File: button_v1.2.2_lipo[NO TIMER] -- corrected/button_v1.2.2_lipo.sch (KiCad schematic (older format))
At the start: 19 parts, among them J1 Conn_01x05_Female, SW1 SW_Push, SW2 SW_Push, U2 AP2112K-3.3, X1 ESP-12E

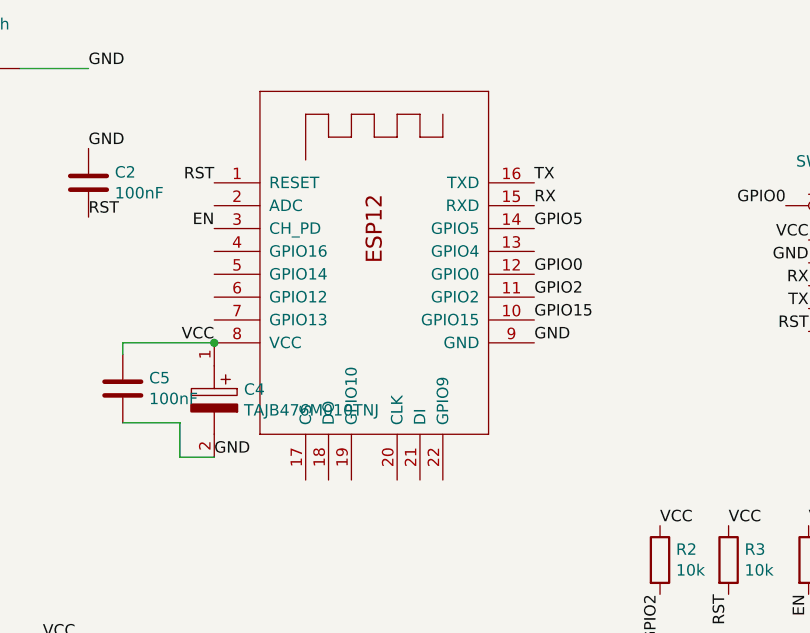
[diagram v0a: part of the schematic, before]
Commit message: All Footprints corrected
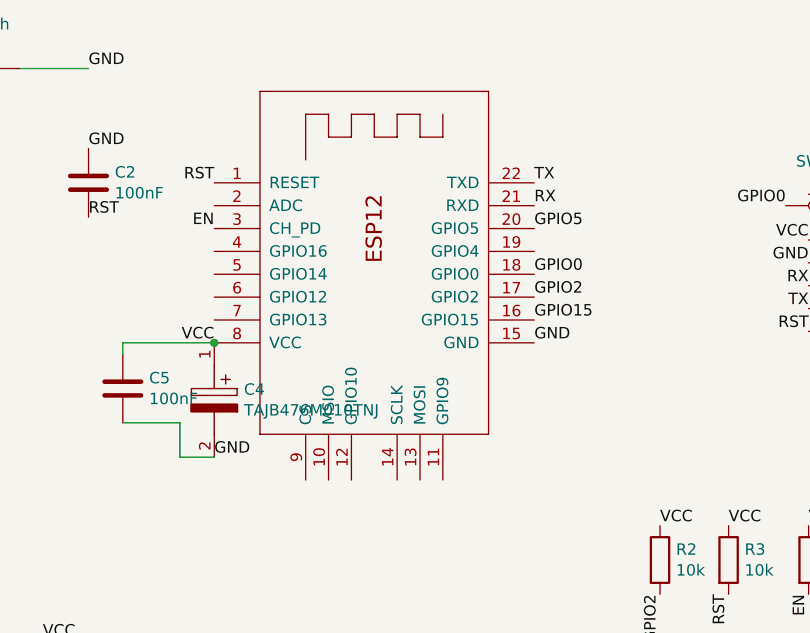
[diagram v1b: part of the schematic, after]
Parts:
- removed X1: ESP-12E, RF_Module:ESP-12E, symbol button_v1.2.2_lipo-rescue:ESP-12E-ardafruit-button-timer-rescue-button-timer-v1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
- added X1: ESP-12E, handsolder:ESP-12Elesssilk, symbol ardafruit:ESP-12E
- D1: footprint LED_SMD:LED_1206_3216Metric_Castellated -> handsolder:LED_1206_3216Metric_Castellated
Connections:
- net EN: now also X1.3 (CH_PD)
- net GND: now also X1.15 (GND)
- net GPIO0: now also X1.18 (GPIO0)
- net GPIO15: now also X1.16 (GPIO15)
- net GPIO2: now also X1.17 (GPIO2)
- net GPIO5: now also X1.20 (GPIO5)
- net RST: now also X1.1 (RESET)
- net RX: now also X1.21 (RXD)
- net TX: now also X1.22 (TXD)
- net VCC: now also X1.8 (VCC)
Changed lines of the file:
@@
 $EndDescr
-$Comp
-L button_v1.2.2_lipo-rescue:ESP-12E-ardafruit-button-timer-rescue-button-timer-v1.2-rescue-button-timer-v1.2-rescue-button-timer-v1.2-rescue-button-timer-v1.2-rescue-button-timer-v1.2-rescue X1
-U 1 1 602C0443
-P 6000 3400
-F 0 "X1" H 6000 3400 50  0001 C CNN
-F 1 "ESP-12E" H 6000 3400 50  0001 C CNN
-F 2 "RF_Module:ESP-12E" H 6000 3400 50  0001 C CNN
-F 3 "" H 6000 3400 50  0001 C CNN
-	1    6000 3400
-	1    0    0    -1
-$EndComp
 $Comp
 L button_v1.2.2_lipo-rescue:Battery_Cell-Device-button-timer-rescue-button-timer-v1.2-rescue-button-timer-v1.2-rescue-button-timer-v1.2-rescue-button-timer-v1.2-rescue-button-timer-v1.2-rescue BT1
@@
 F 0 "D1" V 3547 2378 50  0000 L CNN
 F 1 "LED" V 3638 2378 50  0000 L CNN
-F 2 "LED_SMD:LED_1206_3216Metric_Castellated" H 3600 2300 50  0001 C CNN
+F 2 "handsolder:LED_1206_3216Metric_Castellated" H 3600 2300 50  0001 C CNN
 F 3 "~" H 3600 2300 50  0001 C CNN
 	1    3600 2300
@@
 Wire Wire Line
 	4900 3700 5300 3700
+Wire Wire Line
+	4900 4050 5150 4050
+Wire Wire Line
+	5150 4050 5150 4200
+Wire Wire Line
+	5150 4200 5300 4200
+$Comp
+L ardafruit:ESP-12E X1
+U 1 1 603C2997
+P 6000 3400
+F 0 "X1" H 6000 3400 50  0001 C CNN
+F 1 "ESP-12E" H 6000 3400 50  0001 C CNN
+F 2 "handsolder:ESP-12Elesssilk" H 6000 3400 50  0001 C CNN
+F 3 "" H 6000 3400 50  0001 C CNN
+	1    6000 3400
+	1    0    0    -1
+$EndComp
 Connection ~ 5300 3700
-Wire Wire Line
-	4900 4050 5150 4050
-Wire Wire Line
-	5150 4050 5150 4200
-Wire Wire Line
-	5150 4200 5300 4200
 $EndSCHEMATC
